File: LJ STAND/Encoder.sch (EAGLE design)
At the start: 6 parts, among them IC1 A1301LH, IC2 A1301LH

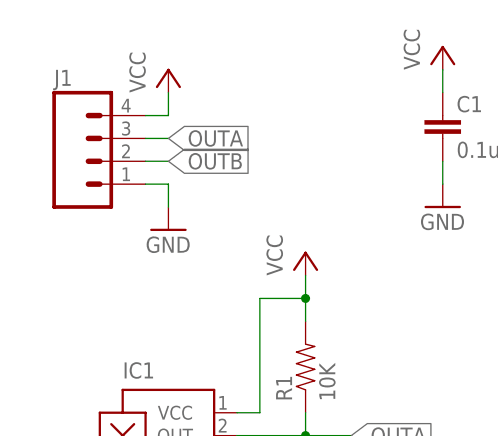
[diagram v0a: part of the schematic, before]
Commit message: Main & light schematics, preliminary board layout
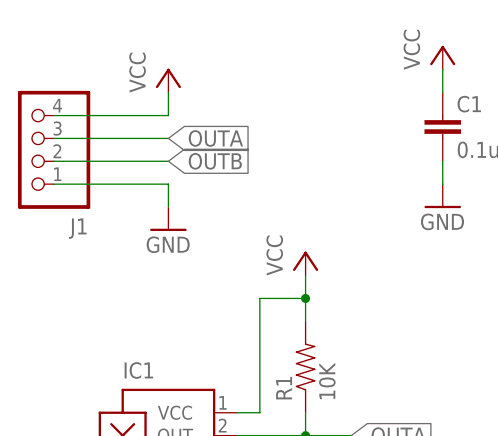
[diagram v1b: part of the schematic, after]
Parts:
- J1: device SparkFun-Connectors:M04PTH -> jst-ph:B4B-PH-K-S
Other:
- moved on the sheet: J1
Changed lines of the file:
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@@
 <?xml version="1.0" encoding="utf-8"?>
 <!DOCTYPE eagle SYSTEM "eagle.dtd">
-<eagle version="8.5.0">
+<eagle version="8.6.3">
 <drawing>
 <settings>
@@
 <part name="GND3" library="supply1" library_urn="urn:adsk.eagle:library:371" deviceset="GND" device=""/>
 <part name="P+2" library="supply1" library_urn="urn:adsk.eagle:library:371" deviceset="VCC" device=""/>
-<part name="J1" library="SparkFun-Connectors" deviceset="M04" device="PTH"/>
+<part name="J1" library="jst-ph" library_urn="urn:adsk.eagle:library:1951258" deviceset="B4B-PH-*" device="K-S" package3d_urn="urn:adsk.eagle:package:1951337/2"/>
 <part name="P+4" library="supply1" library_urn="urn:adsk.eagle:library:371" deviceset="VCC" device=""/>
 <part name="GND4" library="supply1" library_urn="urn:adsk.eagle:library:371" deviceset="GND" device=""/>
@@
 <instance part="GND3" gate="1" x="35.56" y="93.98"/>
 <instance part="P+2" gate="VCC" x="35.56" y="111.76"/>
-<instance part="J1" gate="G$1" x="-2.54" y="99.06"/>
+<instance part="J1" gate="G$1" x="-7.62" y="99.06" rot="R180"/>
 <instance part="P+4" gate="VCC" x="5.08" y="109.22"/>
 <instance part="GND4" gate="1" x="5.08" y="91.44"/>
@@
 <segment>
 <pinref part="J1" gate="G$1" pin="3"/>
-<wire x1="2.54" y1="101.6" x2="5.08" y2="101.6" width="0.1524" layer="91"/>
+<wire x1="-7.62" y1="101.6" x2="5.08" y2="101.6" width="0.1524" layer="91"/>
 <label x="5.08" y="101.6" size="1.778" layer="95" xref="yes"/>
 </segment>
@@
 <segment>
 <pinref part="J1" gate="G$1" pin="2"/>
-<wire x1="2.54" y1="99.06" x2="5.08" y2="99.06" width="0.1524" layer="91"/>
+<wire x1="-7.62" y1="99.06" x2="5.08" y2="99.06" width="0.1524" layer="91"/>
 <label x="5.08" y="99.06" size="1.778" layer="95" xref="yes"/>
 </segment>
@@
 <pinref part="J1" gate="G$1" pin="4"/>
 <pinref part="P+4" gate="VCC" pin="VCC"/>
-<wire x1="2.54" y1="104.14" x2="5.08" y2="104.14" width="0.1524" layer="91"/>
+<wire x1="-7.62" y1="104.14" x2="5.08" y2="104.14" width="0.1524" layer="91"/>
 <wire x1="5.08" y1="104.14" x2="5.08" y2="106.68" width="0.1524" layer="91"/>
 </segment>
@@
 <wire x1="5.08" y1="93.98" x2="5.08" y2="96.52" width="0.1524" layer="91"/>
 <pinref part="J1" gate="G$1" pin="1"/>
-<wire x1="2.54" y1="96.52" x2="5.08" y2="96.52" width="0.1524" layer="91"/>
-</segment>
-</net>
+<wire x1="-7.62" y1="96.52" x2="5.08" y2="96.52" width="0.1524" layer="91"/>
+</segment>
+</net>
